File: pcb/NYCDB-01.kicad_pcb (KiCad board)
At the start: 2 copper layers, 263 parts, among them J1 AUDIO_JACK, J2 AUDIO_JACK, P1 CONN_BATT, P2 USB_OTG, Q1 Q_PMOS_GSD, SW1 SW_POWER, SW2 SW_RESET, U1 CS5361, U10 OPA4134, U11 TPA6120A2, U12 24C16, U13 M25P40, U14 XC6SLX9TQG144, U15 LT1086CT-12, U16 LT1086CT-5, U17 LT3015ET-ADJ, U18 LT3015ET-ADJ, U2 OP1642, U3 OP1642, U4 93CxxA, U5 FT2232D, U6 bq2409x, U7 LTC3521, U8 LT3579, U9 PCM1792A, X1 6MHz, X2 12.288MHz, X3 12.288MHz, X4 12.288MHz

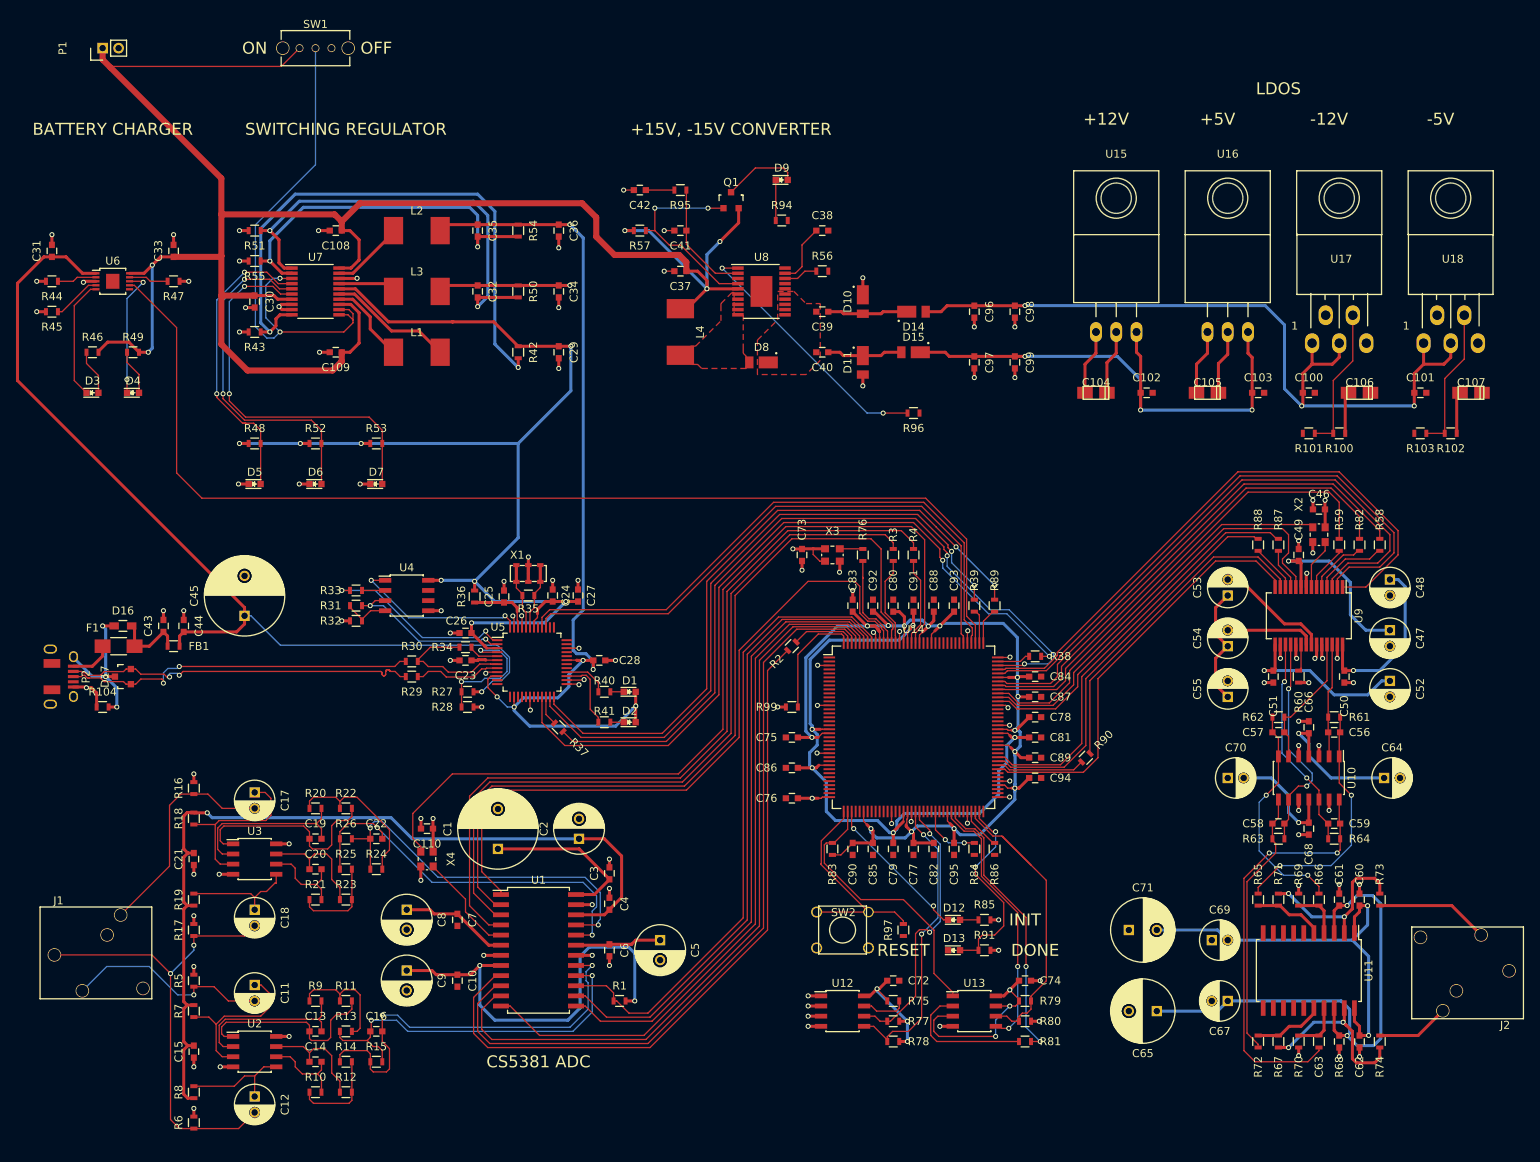
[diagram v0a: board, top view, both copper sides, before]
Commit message: Updated 0603 footprints
Changed to 0603 "handsoldering" versions of the footprints to make my
life easier when assembling everything.  The schematic and PCB
footprints have been updated but the layout hasn't been fixed and
currently fails DRC.
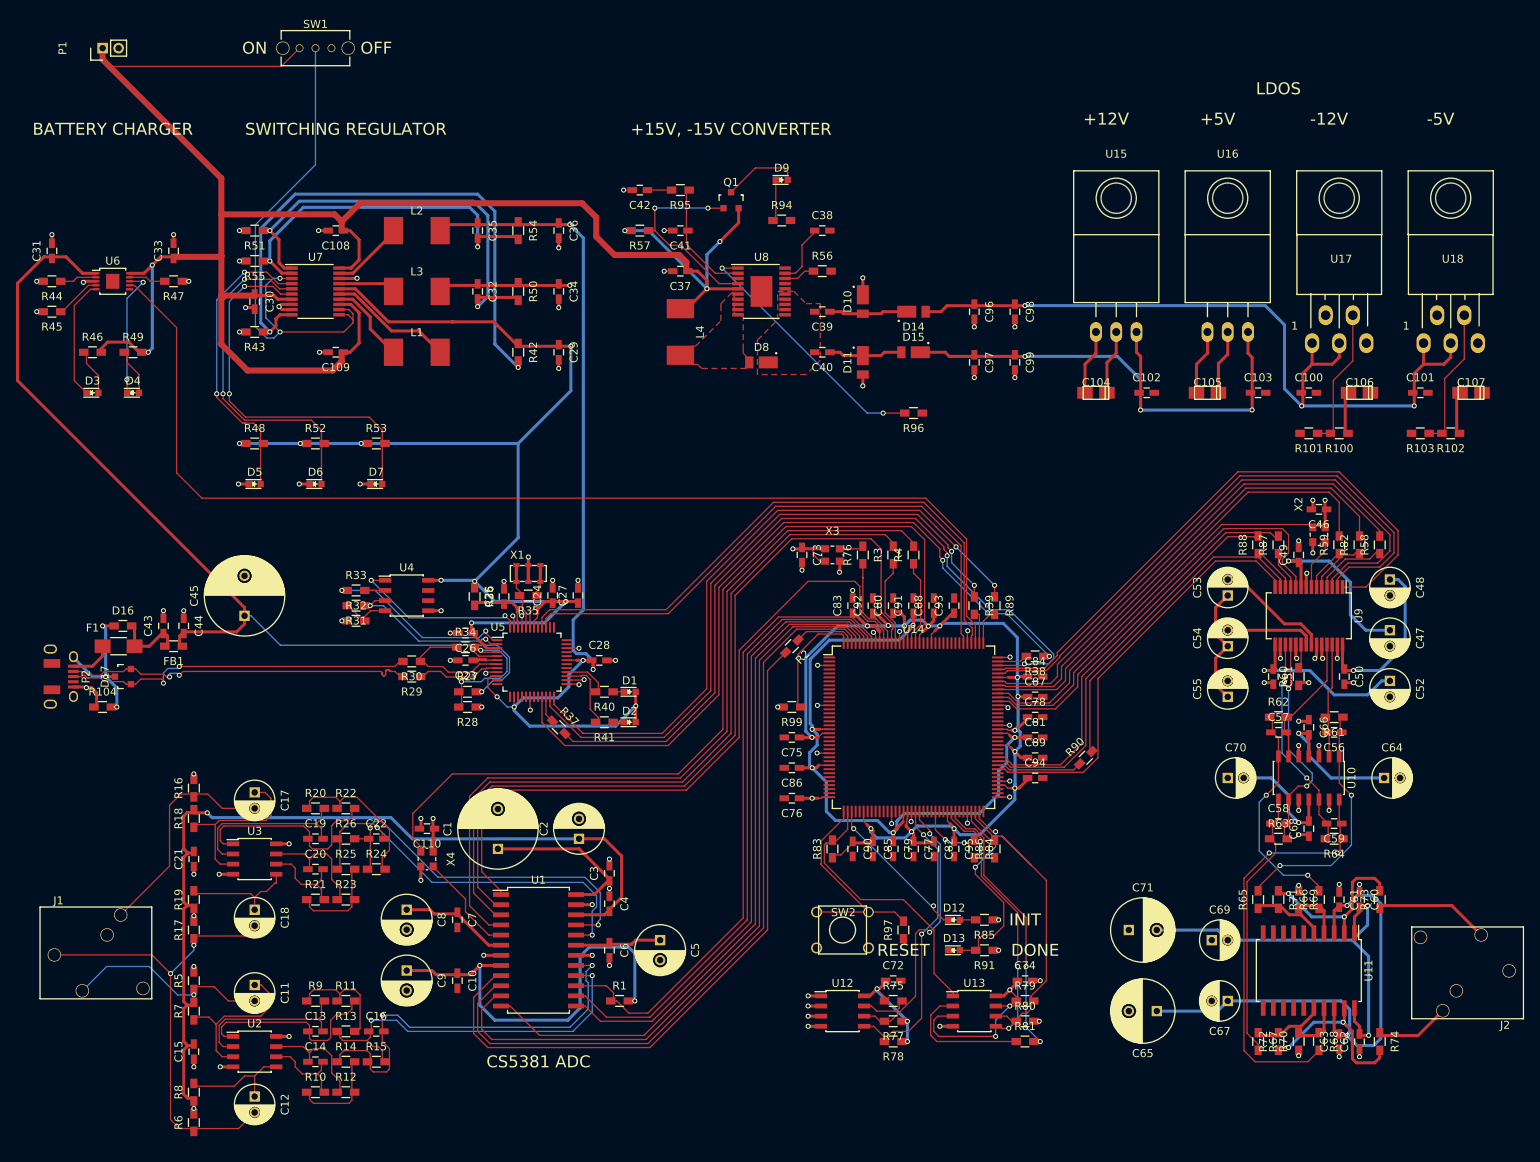
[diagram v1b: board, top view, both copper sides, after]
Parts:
- C10, C100, C101, C102, C103, C108, C109, C110, C13, C14, C15, C16, C19, C20, C21, C22, C23, C24, C25, C26, C27, C28, C29, C3, C30, C31, C32, C33, C34, C35, C36, C37, C38, C39, C4, C40, C41, C42, C43, C44, C46, C49, C50, C51, C56, C57, C58, C59, C6, C60, C61, C62, C63, C66, C68, C7, C72, C73, C74, C75, C76, C77, C78, C79, C80, C81, C82, C83, C84, C85, C86, C87, C88, C89, C90, C91, C92, C93, C94, C95, C96, C97, C98, C99: footprint Capacitors_SMD:C_0603 -> Capacitors_SMD:C_0603_HandSoldering
- FB1, R1, R10, R100, R101, R102, R103, R104, R11, R12, R13, R14, R15, R16, R17, R18, R19, R2, R20, R21, R22, R23, R24, R25, R26, R27, R28, R29, R3, R30, R31, R32, R33, R34, R35, R36, R37, R38, R39, R4, R40, R41, R42, R43, R44, R45, R46, R47, R48, R49, R5, R50, R51, R52, R53, R54, R55, R56, R57, R58, R59, R6, R60, R61, R62, R63, R64, R65, R66, R67, R68, R69, R7, R70, R71, R72, R73, R74, R75, R76, R77, R78, R79, R8, R80, R81, R82, R83, R84, R85, R86, R87, R88, R89, R9, R90, R91, R94, R95, R96, R97, R99: footprint Resistors_SMD:R_0603 -> Resistors_SMD:R_0603_HandSoldering
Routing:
- net /CS5361 ADC/ADC_OVFL: track 80.9 -> 28.7 mm
- net +3V3: track 427.2 -> 479.4 mm
- net Net-(R79-Pad2): track 40.6 -> 10.9 mm
- net Net-(R86-Pad2): track 5.26 -> 35.0 mm
- net Net-(R88-Pad1): track 5.96 -> 15.5 mm
- net /TI DAC/DAC_MDO: track 41.6 -> 32.0 mm

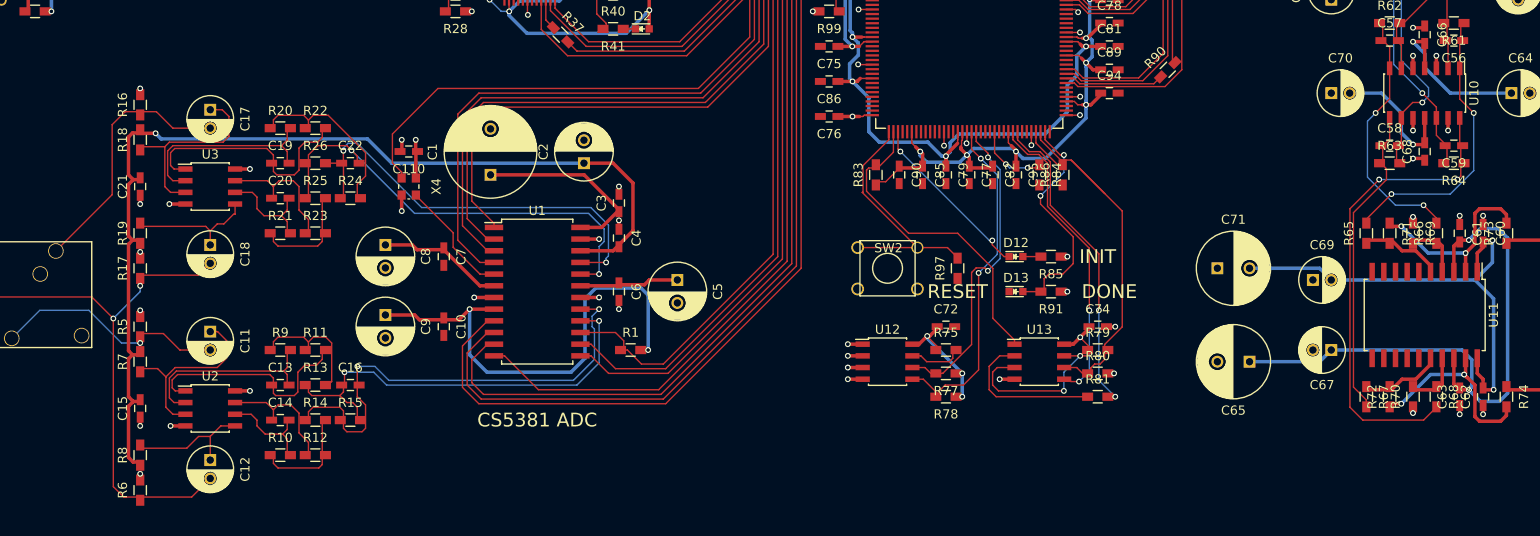
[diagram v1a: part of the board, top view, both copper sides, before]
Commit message: Starting to fix up some of the DRC errors
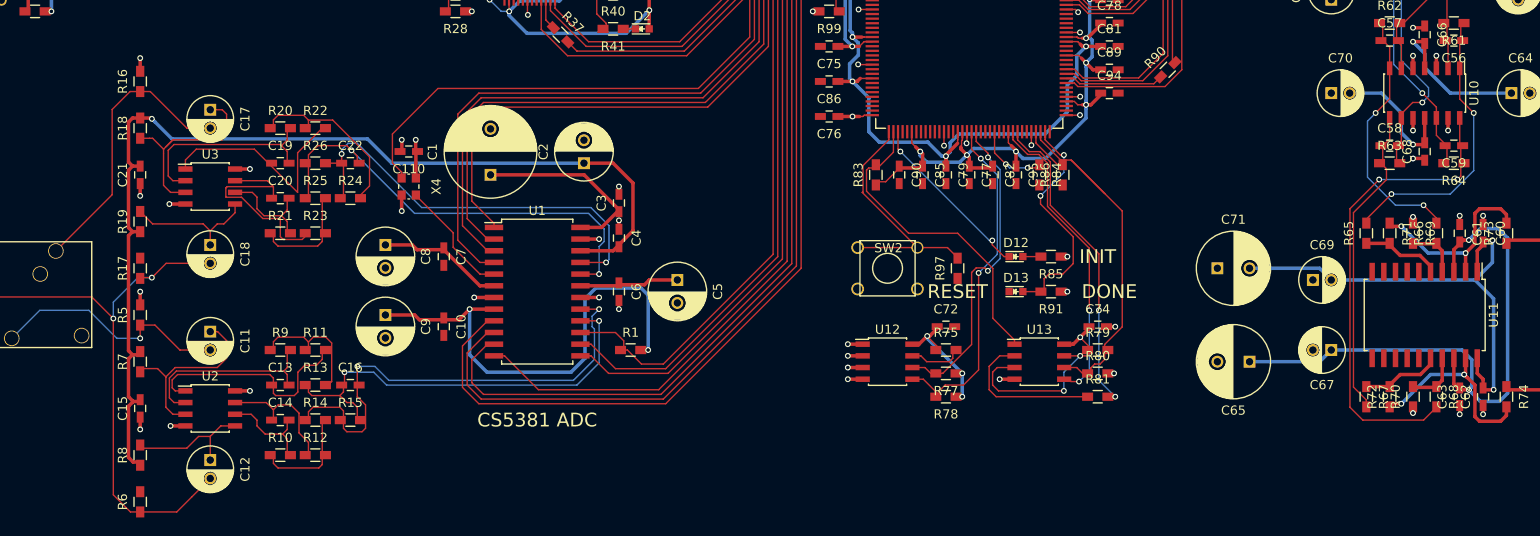
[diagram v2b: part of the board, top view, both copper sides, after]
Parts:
- moved R16 2.54 mm to (41.9, 108.0)
- moved R5 1.27 mm to (41.9, 133.3)
- moved C21 1.27 mm to (41.9, 118.1)
- moved R18 1.27 mm to (41.9, 113.0)
- moved R19 1.27 mm to (41.9, 123.2)
- moved R6 1.27 mm to (41.9, 153.7)
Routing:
- net Net-(R86-Pad2): track 35.0 -> 9.51 mm
- net Net-(R79-Pad2): track 10.9 -> 36.3 mm
- net Net-(R88-Pad1): track 15.5 -> 37.4 mm
- net /TI DAC/DAC_MDO: track 32.0 -> 10.1 mm
- net Net-(C20-Pad1): track 14.5 -> 24.2 mm
- net /CS5361 ADC/ING: track 59.7 -> 62.9 mm
- net /CS5361 ADC/INR: track 28.3 -> 31.1 mm
- net Net-(C19-Pad1): track 26.2 -> 23.7 mm
- net /CS5361 ADC/left buffer/VQ: track 111.0 -> 112.5 mm
- net Net-(C17-Pad1): track 21.5 -> 22.5 mm
- net GND: track 171.7 -> 170.9 mm, vias 109 -> 107
- net Net-(R65-Pad1): track 8.81 -> 9.60 mm
- net /CS5361 ADC/INL: track 26.1 -> 26.7 mm
- net Net-(C18-Pad1): track 13.9 -> 14.5 mm

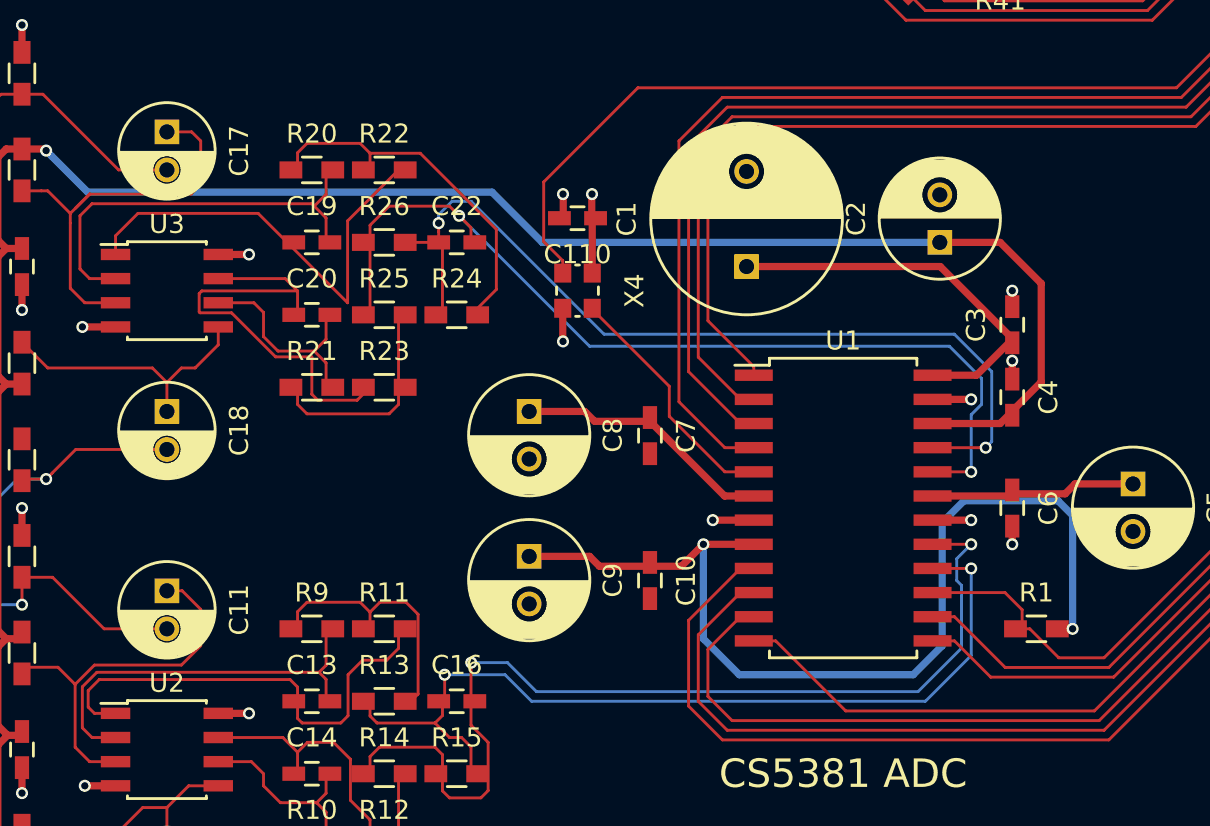
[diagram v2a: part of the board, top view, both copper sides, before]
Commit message: Fixing up some tracks
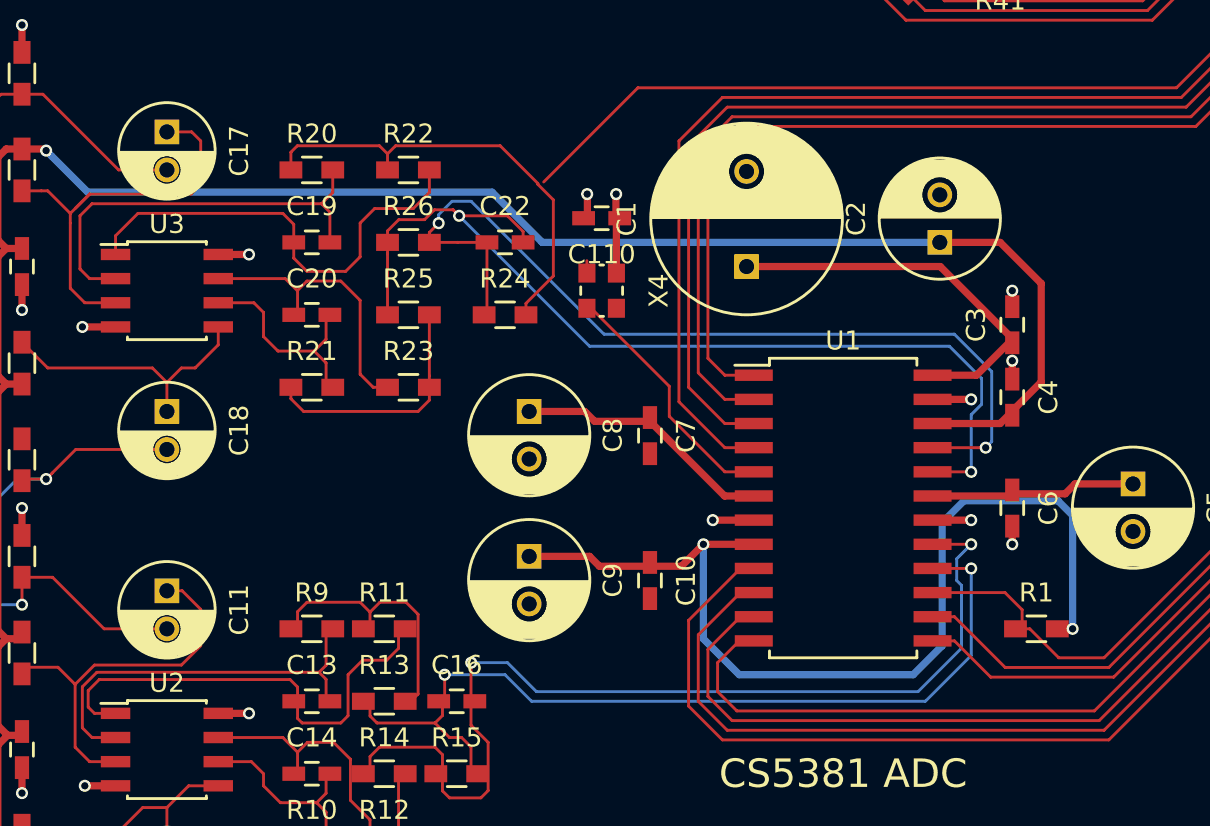
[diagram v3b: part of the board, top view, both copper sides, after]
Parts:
- moved C22 2.54 mm to (67.3, 116.8)
- moved R24 2.54 mm to (67.3, 120.7)
- moved C110 1.27 mm to (72.4, 115.6)
- moved R22 1.27 mm to (62.2, 113.0)
- moved R23 1.27 mm to (62.2, 124.5)
- moved R25 1.27 mm to (62.2, 120.7)
- moved R26 1.27 mm to (62.2, 116.8)
- moved X4 1.27 mm to (72.4, 119.4)
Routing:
- net Net-(C20-Pad1): track 24.2 -> 15.2 mm
- net /CS5361 ADC/ADC_I2S_LJ: track 88.8 -> 93.5 mm
- net Net-(R20-Pad1): track 19.4 -> 23.9 mm
- net /CS5361 ADC/ADC_MCLK_EN: track 108.6 -> 104.0 mm
- net GND: track 170.9 -> 169.1 mm, vias 107 -> 106
- net Net-(R21-Pad1): track 11.3 -> 12.9 mm
- net /CS5361 ADC/right buffer/AIN-: track 49.9 -> 51.2 mm
- net /CS5361 ADC/right buffer/AIN+: track 47.7 -> 48.6 mm
- net /CS5361 ADC/ADC_RST: track 87.6 -> 88.5 mm
- net Net-(C19-Pad1): track 23.7 -> 24.2 mm

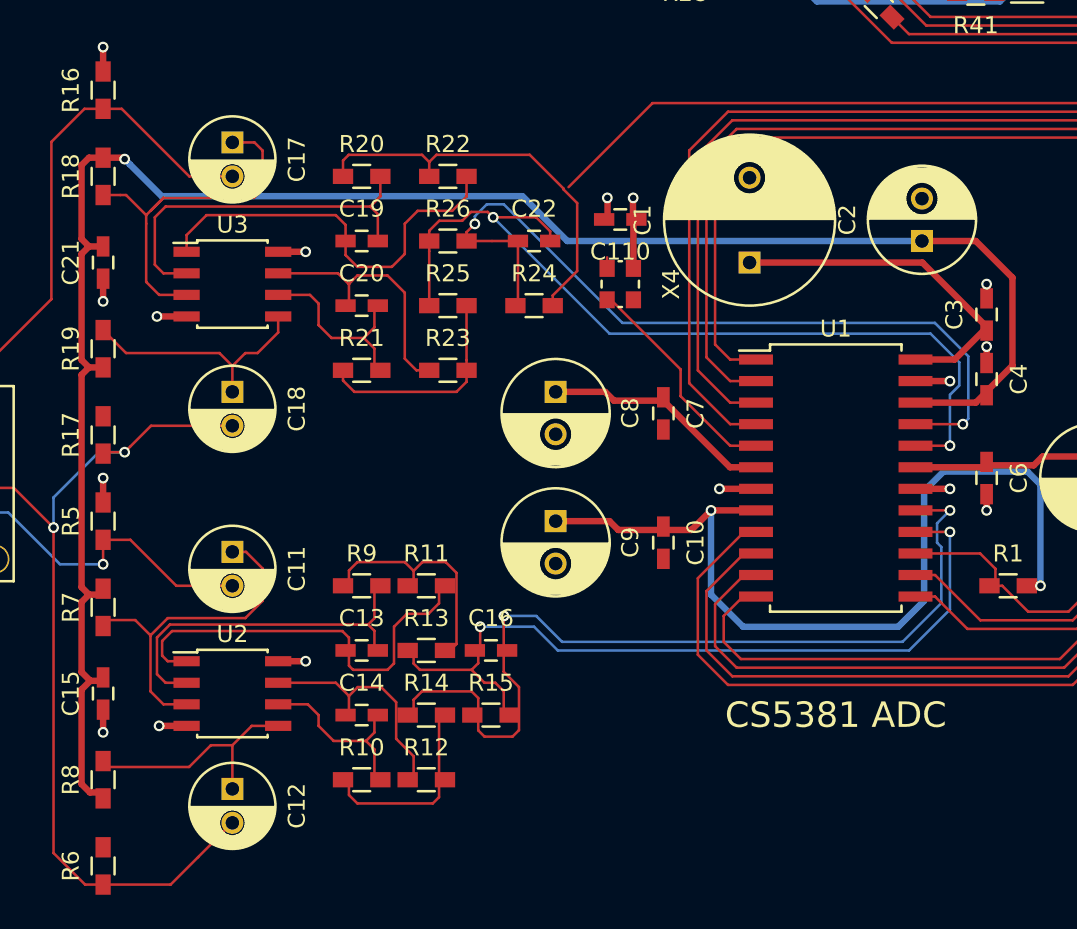
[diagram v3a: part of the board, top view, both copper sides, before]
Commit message: Cleaned up a lot of the ADC input tracks
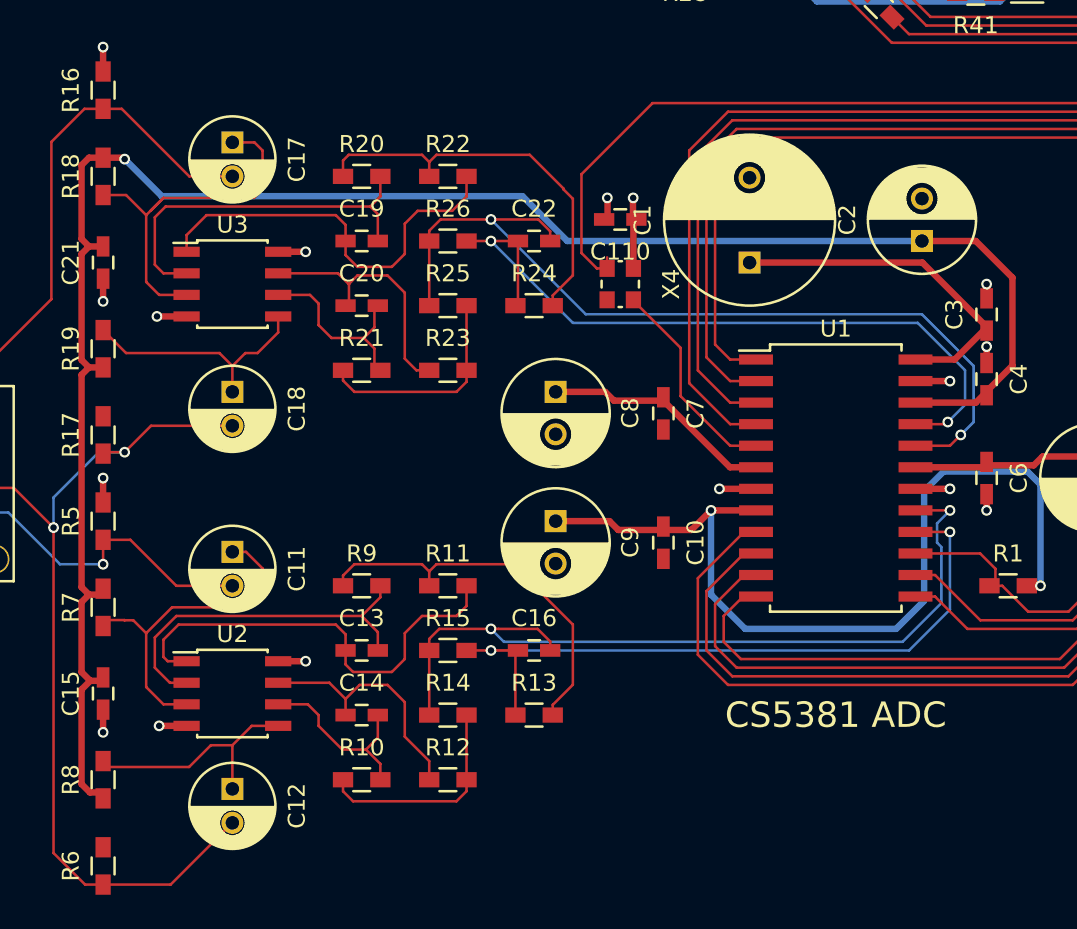
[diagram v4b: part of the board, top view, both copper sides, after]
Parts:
- moved R13 7.41 mm to (67.3, 144.8)
- moved R15 4.58 mm to (62.2, 141.0)
- moved C16 2.54 mm to (67.3, 141.0)
- moved R11 1.27 mm to (62.2, 137.2)
- moved R12 1.27 mm to (62.2, 148.6)
- moved R14 1.27 mm to (62.2, 144.8)
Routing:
- net Net-(R11-Pad1): track 14.4 -> 22.9 mm
- net /CS5361 ADC/ADC_MCLK_EN: track 104.0 -> 109.5 mm
- net /CS5361 ADC/left buffer/AIN+: track 46.8 -> 41.6 mm
- net /CS5361 ADC/right buffer/AIN+: track 48.6 -> 43.4 mm
- net /CS5361 ADC/left buffer/AIN-: track 52.1 -> 48.4 mm
- net Net-(C13-Pad1): track 24.8 -> 26.6 mm
- net Net-(R10-Pad1): track 11.4 -> 12.9 mm
- net /CS5361 ADC/right buffer/AIN-: track 51.2 -> 52.0 mm
- net Net-(C14-Pad1): track 14.0 -> 14.7 mm
- net Net-(U1-Pad5): track 13.0 -> 12.5 mm
